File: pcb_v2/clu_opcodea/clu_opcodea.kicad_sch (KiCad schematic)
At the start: 33 parts, among them J1 UCODE, U1 74LS00

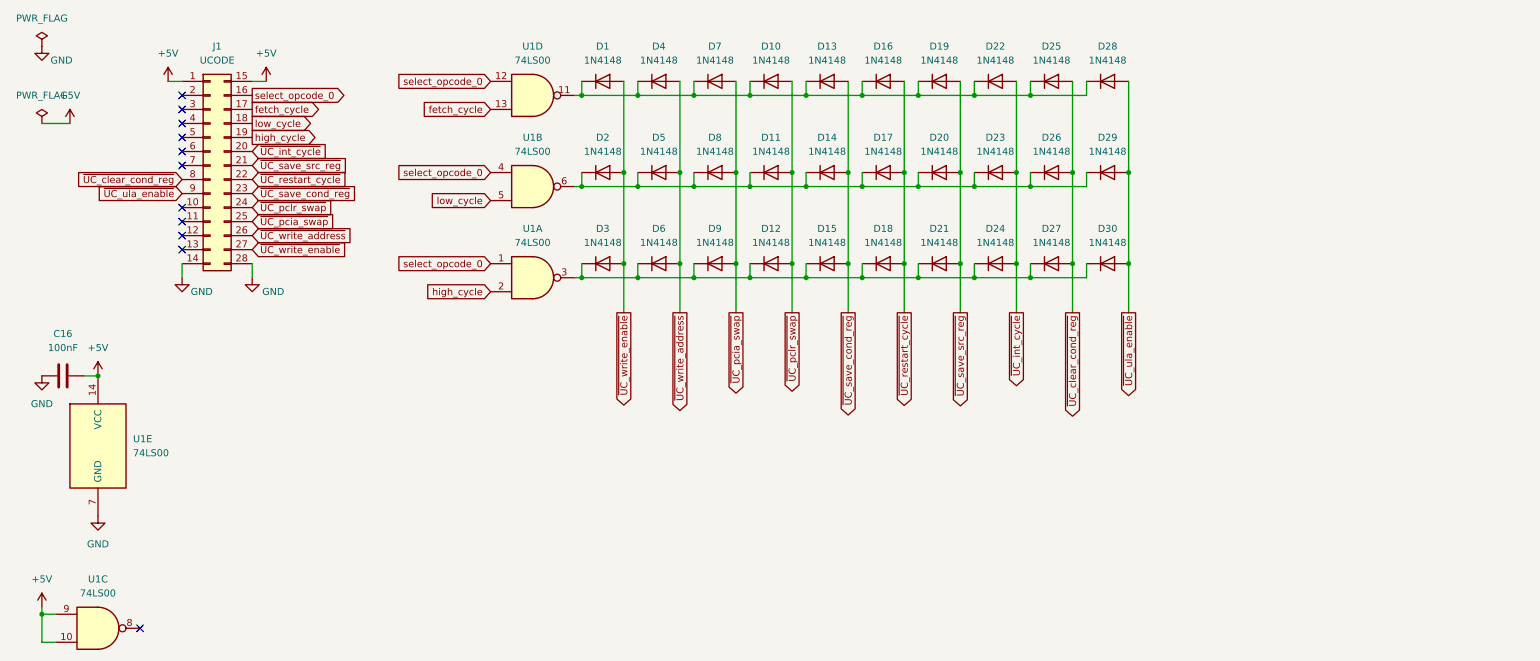
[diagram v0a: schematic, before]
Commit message: continuando com a implementação da lógica de controle; ROM de ucode expandida para 17 bits
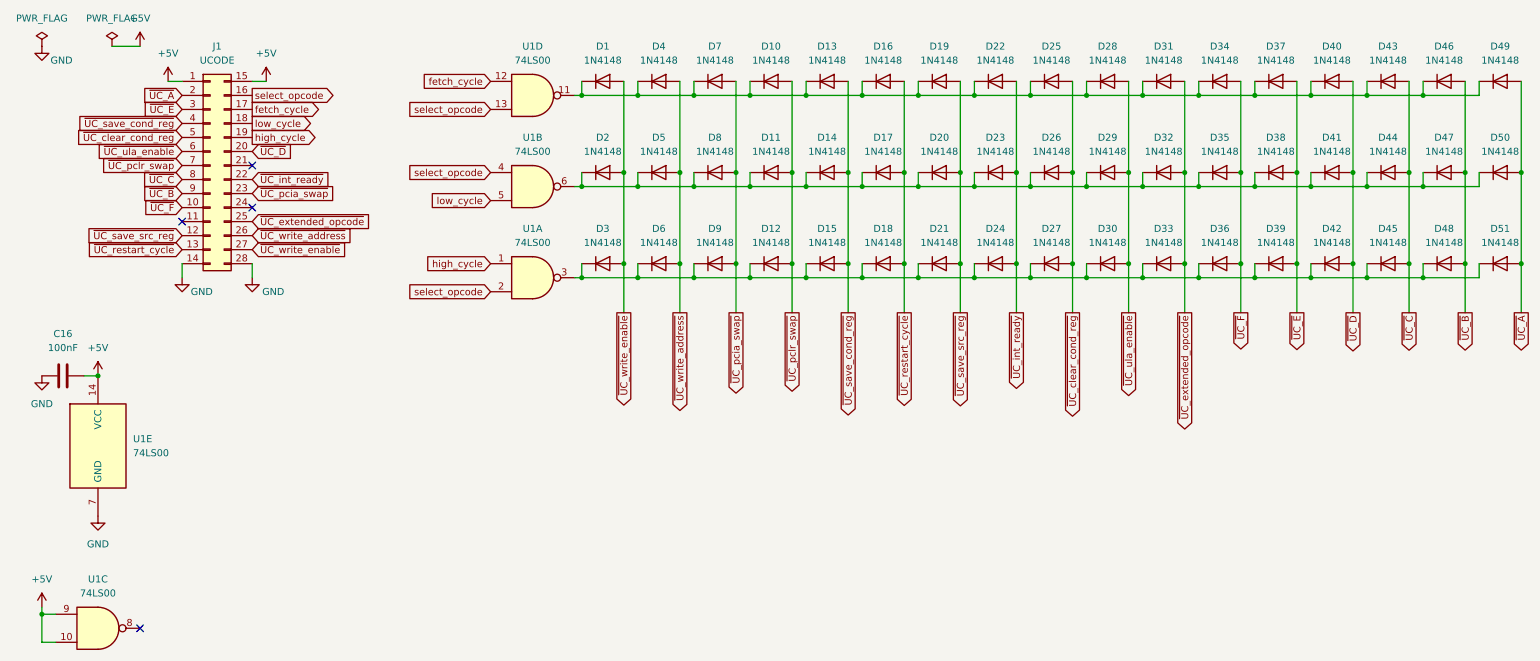
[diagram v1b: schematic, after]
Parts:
- added D31, D32, D33, D34, D35, D36, D37, D38, D39, D40, D41, D42, D43, D44, D45, D46, D47, D48, D49, D50, D51: 1N4148, Diode_THT:D_DO-35_SOD27_P2.54mm_Vertical_AnodeUp, symbol Diode:1N4148
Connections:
- net fetch_cycle: now also U1.12; no longer U1.13
- net high_cycle: now also U1.1; no longer U1.2
- net ~{UC_clear_cond_reg}: now also J1.5 (Pin_5); no longer J1.8 (Pin_8)
- net ~{UC_pcia_swap}: now also J1.23 (Pin_23); no longer J1.25 (Pin_25)
- net ~{UC_pclr_swap}: now also J1.7 (Pin_7); no longer J1.24 (Pin_24)
- net ~{UC_restart_cycle}: now also J1.13 (Pin_13); no longer J1.22 (Pin_22)
- net ~{UC_save_cond_reg}: now also J1.4 (Pin_4); no longer J1.23 (Pin_23)
- net ~{UC_save_src_reg}: now also J1.12 (Pin_12); no longer J1.21 (Pin_21)
- net ~{UC_ula_enable}: now also J1.6 (Pin_6); no longer J1.9 (Pin_9)
- net at D11.1 (K), D14.1 (K), D17.1 (K)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: now also D32.1 (K), D35.1 (K), D38.1 (K), D41.1 (K), D44.1 (K), D47.1 (K), D50.1 (K)
- net at D1.1 (K), D10.1 (K), D13.1 (K)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: now also D31.1 (K), D34.1 (K), D37.1 (K), D40.1 (K), D43.1 (K), D46.1 (K), D49.1 (K)
- net at D12.1 (K), D15.1 (K), D18.1 (K)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: now also D33.1 (K), D36.1 (K), D39.1 (K), D42.1 (K), D45.1 (K), D48.1 (K), D51.1 (K)
- net ~{UC_F}: now reaches J1.10 (Pin_10)
- net ~{UC_F}: now also D34.2 (A), D35.2 (A), D36.2 (A)
- net ~{UC_A}: now reaches J1.2 (Pin_2)
- net ~{UC_A}: now also D49.2 (A), D50.2 (A), D51.2 (A)
- net ~{UC_E}: now reaches J1.3 (Pin_3)
- net ~{UC_E}: now also D37.2 (A), D38.2 (A), D39.2 (A)
- net select_opcode_0 renamed select_opcode
- net select_opcode: now also U1.13, U1.2; no longer U1.1, U1.12
- net ~{UC_int_cycle} renamed ~{UC_int_ready}
- net ~{UC_int_ready}: now also J1.22 (Pin_22); no longer J1.20 (Pin_20)
- new net ~{UC_B}: D46.2 (A), D47.2 (A), D48.2 (A), J1.9 (Pin_9)
- new net ~{UC_C}: D43.2 (A), D44.2 (A), D45.2 (A), J1.8 (Pin_8)
- new net ~{UC_D}: D40.2 (A), D41.2 (A), D42.2 (A), J1.20 (Pin_20)
- new net ~{UC_extended_opcode}: D31.2 (A), D32.2 (A), D33.2 (A), J1.25 (Pin_25)
- no-connect marks 11 -> 4

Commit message: alteração de layout
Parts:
- removed D43, D44, D45, D46, D47, D48, D49, D50, D51: 1N4148, Diode_THT:D_DO-35_SOD27_P2.54mm_Vertical_AnodeUp, symbol Diode:1N4148
- renumbered C16 to C1
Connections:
- net fetch_cycle: now also J1.16 (Pin_16); no longer J1.17 (Pin_17)
- net high_cycle: now also J1.17 (Pin_17); no longer J1.19 (Pin_19)
- net select_opcode: now also J1.19 (Pin_19); no longer J1.16 (Pin_16)
- net ~{UC_A}: now also D40.2 (A), D41.2 (A), D42.2 (A), J1.24 (Pin_24); no longer J1.2 (Pin_2)
- net ~{UC_B}: now also D37.2 (A), D38.2 (A), D39.2 (A)
- net ~{UC_C}: now also D34.2 (A), D35.2 (A), D36.2 (A), J1.11 (Pin_11); no longer J1.8 (Pin_8)
- net ~{UC_D}: now also D10.2 (A), D11.2 (A), D12.2 (A), J1.27 (Pin_27); no longer D40.2 (A), D41.2 (A), D42.2 (A), J1.20 (Pin_20)
- net ~{UC_clear_cond_reg}: now also J1.26 (Pin_26); no longer J1.5 (Pin_5)
- net ~{UC_extended_opcode}: now also J1.6 (Pin_6); no longer J1.25 (Pin_25)
- net ~{UC_restart_cycle}: now also J1.12 (Pin_12); no longer J1.13 (Pin_13)
- net ~{UC_save_cond_reg}: now also J1.20 (Pin_20); no longer J1.4 (Pin_4)
- net ~{UC_save_src_reg}: now also J1.25 (Pin_25); no longer J1.12 (Pin_12)
- net ~{UC_ula_enable}: now also J1.8 (Pin_8); no longer J1.6 (Pin_6)
- net ~{UC_write_address}: now also J1.13 (Pin_13); no longer J1.26 (Pin_26)
- net ~{UC_write_enable}: now also J1.21 (Pin_21); no longer J1.27 (Pin_27)
- removed net ~{UC_E}: D37.2 (A), D38.2 (A), D39.2 (A), J1.3 (Pin_3)
- removed net ~{UC_F}: D34.2 (A), D35.2 (A), D36.2 (A), J1.10 (Pin_10)
- removed net ~{UC_pclr_swap}: D10.2 (A), D11.2 (A), D12.2 (A), J1.7 (Pin_7)
- no-connect marks 4 -> 7

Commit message: revisando o ERC
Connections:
- net ~{UC_D} renamed ~{UC_read_addr_src_reg}
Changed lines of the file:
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@@
 		)
 	)
-	(global_label "~{UC_D}"
+	(global_label "~{UC_read_addr_src_reg}"
 		(shape input)
 		(at 58.42 58.42 0)
@@
 		)
 		(property "Intersheetrefs" "${INTERSHEET_REFS}"
-			(at 66.2433 58.42 0)
+			(at 82.2088 58.42 0)
 			(effects
 				(font
@@
 		)
 	)
-	(global_label "~{UC_D}"
+	(global_label "~{UC_read_addr_src_reg}"
 		(shape output)
 		(at 156.21 69.85 270)
@@
 		)
 		(property "Intersheetrefs" "${INTERSHEET_REFS}"
-			(at 156.21 77.6733 90)
-			(effects
-				(font
+			(at 156.21 93.6388 90)
+			(effects
+				(font

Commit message: novos sinais
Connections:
- net ~{UC_B} renamed ~{UC_read_mem_const}
- net ~{UC_C} renamed ~{UC_const_boot_addr}
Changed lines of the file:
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@@
 		)
 	)
+	(global_label "~{UC_const_boot_addr}"
+		(shape output)
+		(at 237.49 69.85 270)
+		(fields_autoplaced yes)
+		(effects
+			(font
+				(size 1.27 1.27)
+			)
+			(justify right)
+		)
+		(property "Intersheetrefs" "${INTERSHEET_REFS}"
+			(at 237.49 91.8848 90)
+			(effects
+				(font
+					(size 1.27 1.27)
+				)
+				(justify right)
+				(hide yes)
+			)
+		)
+	)
+	(global_label "~{UC_read_mem_const}"
+		(shape output)
+		(at 247.65 69.85 270)
+		(fields_autoplaced yes)
+		(effects
+			(font
+				(size 1.27 1.27)
+			)
+			(justify right)
+		)
+		(property "Intersheetrefs" "${INTERSHEET_REFS}"
+			(at 247.65 92.1269 90)
+			(effects
+				(font
+					(size 1.27 1.27)
+				)
+				(justify right)
+				(hide yes)
+			)
+		)
+	)
 	(global_label "~{UC_write_address}"
 		(shape output)
@@
 		)
 	)
-	(global_label "~{UC_save_src_reg}"
+	(global_label "~{UC_const_boot_addr}"
 		(shape input)
-		(at 58.42 53.34 0)
+		(at 45.72 53.34 180)
 		(fields_autoplaced yes)
 		(effects
@@
 				(size 1.27 1.27)
 			)
-			(justify left)
+			(justify right)
 		)
 		(property "Intersheetrefs" "${INTERSHEET_REFS}"
-			(at 77.0685 53.34 0)
+			(at 23.6852 53.34 0)
 			(effects
 				(font
 					(size 1.27 1.27)
 				)
-				(justify left)
+				(justify right)
 				(hide yes)
 			)
 		)
 	)
-	(global_label "high_cycle"
-		(shape output)
-		(at 58.42 33.02 0)
+	(global_label "~{UC_save_src_reg}"
+		(shape input)
+		(at 58.42 53.34 0)
 		(fields_autoplaced yes)
 		(effects
@@
 		)
 		(property "Intersheetrefs" "${INTERSHEET_REFS}"
-			(at 71.3232 33.02 0)
+			(at 77.0685 53.34 0)
 			(effects
 				(font
@@
 		)
 	)
-	(global_label "~{UC_B}"
+	(global_label "high_cycle"
 		(shape output)
-		(at 247.65 69.85 270)
-		(fields_autoplaced yes)
-		(effects
-			(font
-				(size 1.27 1.27)
-			)
-			(justify right)
-		)
-		(property "Intersheetrefs" "${INTERSHEET_REFS}"
-			(at 247.65 77.6733 90)
-			(effects
-				(font
-					(size 1.27 1.27)
-				)
-				(justify right)
-				(hide yes)
-			)
-		)
-	)
-	(global_label "~{UC_B}"
-		(shape input)
-		(at 45.72 48.26 180)
+		(at 58.42 33.02 0)
 		(fields_autoplaced yes)
 		(effects
@@
 				(size 1.27 1.27)
 			)
-			(justify right)
+			(justify left)
 		)
 		(property "Intersheetrefs" "${INTERSHEET_REFS}"
-			(at 37.8967 48.26 0)
+			(at 71.3232 33.02 0)
 			(effects
 				(font
 					(size 1.27 1.27)
 				)
-				(justify right)
+				(justify left)
 				(hide yes)
 			)
@@
 		)
 	)
-	(global_label "~{UC_C}"
-		(shape output)
-		(at 237.49 69.85 270)
+	(global_label "~{UC_read_mem_const}"
+		(shape input)
+		(at 45.72 48.26 180)
 		(fields_autoplaced yes)
 		(effects
@@
 		)
 		(property "Intersheetrefs" "${INTERSHEET_REFS}"
-			(at 237.49 77.6733 90)
+			(at 23.4431 48.26 0)
 			(effects
 				(font
@@
 		)
 	)
-	(global_label "~{UC_C}"
-		(shape input)
-		(at 45.72 53.34 180)
-		(fields_autoplaced yes)
-		(effects
-			(font
-				(size 1.27 1.27)
-			)
-			(justify right)
-		)
-		(property "Intersheetrefs" "${INTERSHEET_REFS}"
-			(at 37.8967 53.34 0)
-			(effects
-				(font
-					(size 1.27 1.27)
-				)
-				(justify right)
-				(hide yes)
-			)
-		)
-	)
 	(global_label "~{UC_restart_cycle}"
 		(shape output)
@@
 		)
 		(instances
-			(project ""
+			(project "clu_opcodea"
 				(path "/339691d7-f136-4bdc-bb08-dd33e05336a9"
 					(reference "U1")
@@
 		)
 		(instances
-			(project ""
+			(project "clu_opcodea"
 				(path "/339691d7-f136-4bdc-bb08-dd33e05336a9"
 					(reference "U1")
@@
 		)
 		(instances
-			(project ""
+			(project "clu_opcodea"
 				(path "/339691d7-f136-4bdc-bb08-dd33e05336a9"
 					(reference "U1")
@@
 		)
 		(instances
-			(project ""
+			(project "clu_opcodea"
 				(path "/339691d7-f136-4bdc-bb08-dd33e05336a9"
 					(reference "#FLG01")
@@
 		)
 		(instances
-			(project ""
+			(project "clu_opcodea"
 				(path "/339691d7-f136-4bdc-bb08-dd33e05336a9"
 					(reference "U1")
@@
 		)
 		(instances
-			(project ""
+			(project "clu_opcodea"
 				(path "/339691d7-f136-4bdc-bb08-dd33e05336a9"
 					(reference "D1")
@@
 		)
 		(instances
-			(project ""
+			(project "clu_opcodea"
 				(path "/339691d7-f136-4bdc-bb08-dd33e05336a9"
 					(reference "U1")
